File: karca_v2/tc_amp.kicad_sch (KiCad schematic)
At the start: 12 parts, among them U20 AD8495

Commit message: updated
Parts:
- removed C28: 0.82u, Capacitor_SMD:C_1206_3216Metric, symbol Device:C
- removed L6: 4.7m, symbol Device:L
- added C9: 0.075u, Capacitor_SMD:C_1206_3216Metric, symbol Device:C
- added Ce1: 0.15u, Capacitor_SMD:C_1206_3216Metric, symbol Device:C
- added D25: D_Schottky, Diode_SMD:D_SMA, symbol Device:D_Schottky
- added D58, D62: TVS0701, symbol Device:D_TVS
- added R61: 1k, symbol Device:R_US
- added U43: TLV9304xD, Package_SO:SO-14_3.9x8.65mm_P1.27mm, symbol Amplifier_Operational:TLV9304xD
- R57: value 90 -> 1k
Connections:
- net +5V: now also D25.1 (K)
- net GND: now also C9.2, D58.1 (A1), D62.1 (A1)
- net IN_1: now also D58.2 (A2)
- net IN_2: now also D62.2 (A2)
- net V_OUT: now also Ce1.1, D25.2 (A), U43.6 (-), U43.7
- net at R57.2: now also Ce1.2, R61.1
- new net: C9.1, R61.2, U43.5 (+)
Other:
- note added: "fc = 1.5kHz"
- note removed: "Inductor has 20 ohms of resistance"
- note removed: "fc = 2.5kHz"

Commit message: Version alpha
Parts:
- removed D25: D_Schottky, Diode_SMD:D_SMA, symbol Device:D_Schottky
- removed D58, D62: TVS0701, symbol Device:D_TVS
- added R116: 1k, Resistor_SMD:R_1206_3216Metric, symbol Device:R_US
- added U25: ~, Package_SON:VSON-8-1EP_3x3mm_P0.65mm_EP1.65x2.4mm_ThermalVias, symbol karca_lib:TVS0701-7V
- added U39: ~, Package_TO_SOT_SMD:SOT-23-5, symbol karca_lib:TLVH431
- C26, C29: footprint Capacitor_SMD:C_1210_3225Metric -> Capacitor_SMD:C_1206_3216Metric
- R57: renamed from R56; footprint (none) -> Resistor_SMD:R_1206_3216Metric
- R58: renamed from R57; footprint (none) -> Resistor_SMD:R_1206_3216Metric
- R59: renamed from R61; footprint (none) -> Resistor_SMD:R_1206_3216Metric
- R60: renamed from R58; footprint (none) -> Resistor_SMD:R_1206_3216Metric
- R61: renamed from R59; footprint (none) -> Resistor_SMD:R_1206_3216Metric
- renumbered C9 to C28, U43 to U13, U20 to U24
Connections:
- net +5V: now also R116.2
- net GND: now also U25.5 (GND), U25.6 (GND), U39.5 (A); no longer U24.2 (REF)
- net IN_1: now also U25.1 (IN)
- net IN_2: now also U25.2 (IN)
- new net: R116.1, U24.2 (REF), U39.3 (C), U39.4 (REF)
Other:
- note removed: "Vref set to 0V since only +ve temperatures will be measured"
- moved on the sheet: C25, C26, C27, C28, C29, C30, Ce1, R57, R58, R59, R60, R61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

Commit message: discrete traces
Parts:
- renumbered C25 to C40, C26 to C41, C27 to C42, C28 to C43, C29 to C44, C30 to C45, R116 to R62, U24 to U30, U25 to U31, U39 to U37

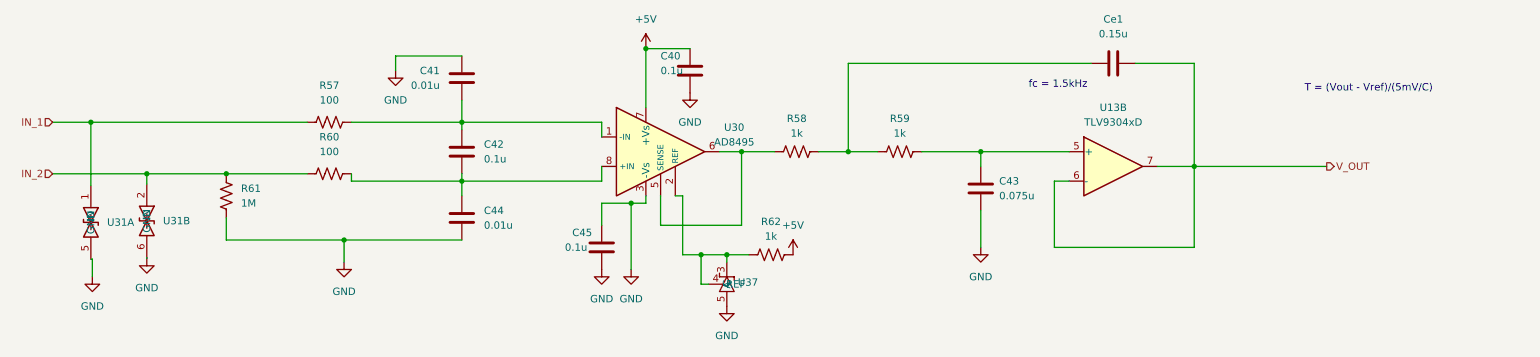
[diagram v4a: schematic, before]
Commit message: fixed TVS Diodes
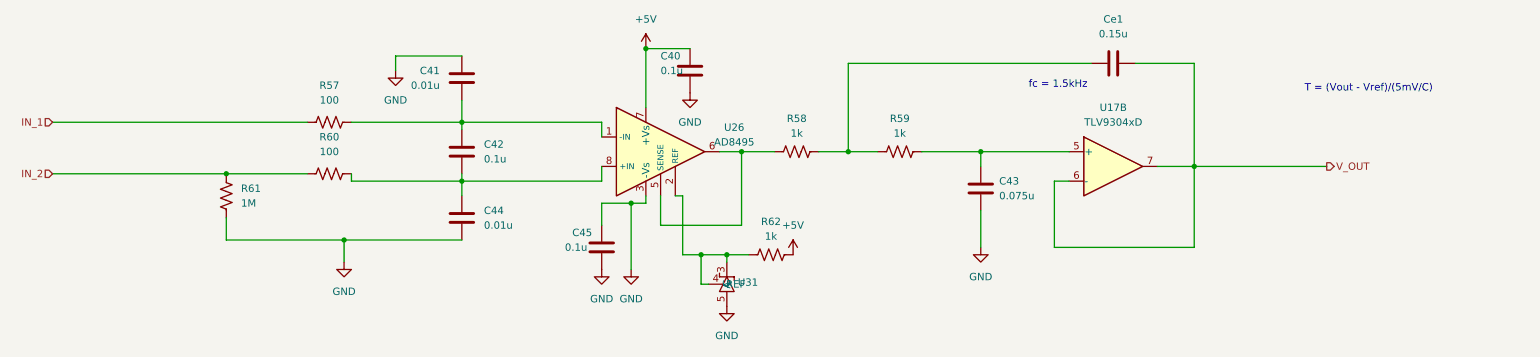
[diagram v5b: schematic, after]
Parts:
- removed U31: ~, Package_SON:VSON-8-1EP_3x3mm_P0.65mm_EP1.65x2.4mm_ThermalVias, symbol karca_lib:TVS0701-7V
- renumbered U13 to U17, U30 to U26, U37 to U31

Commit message: fixed violations
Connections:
- net in+: now reaches C42.1, C44.2, R60.2, U26.8 (+IN)
- net in-: now reaches C41.1, C42.2, R57.2, U26.1 (-IN)
- net vref: now reaches R62.1, U26.2 (REF), U31.3 (C), U31.4 (REF)
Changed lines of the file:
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@@
+    (effects (font (size 1.27 1.27)) (justify left bottom))
+  )
+  (label "vref" (at 140.97 62.23 0) (fields_autoplaced)
+    (effects (font (size 1.27 1.27)) (justify left bottom))
+  )
+  (label "in-" (at 125.095 49.53 0) (fields_autoplaced)
+    (effects (font (size 1.27 1.27)) (justify left bottom))
+  )
+  (label "in+" (at 123.825 59.69 0) (fields_autoplaced)
     (effects (font (size 1.27 1.27)) (justify left bottom))
   )

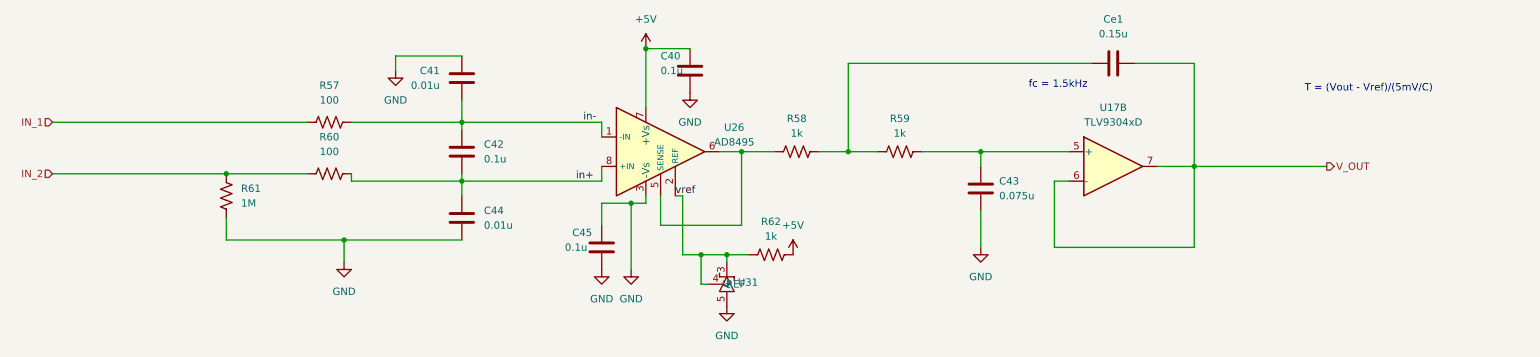
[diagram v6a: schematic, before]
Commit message: Fixed ground capacitors
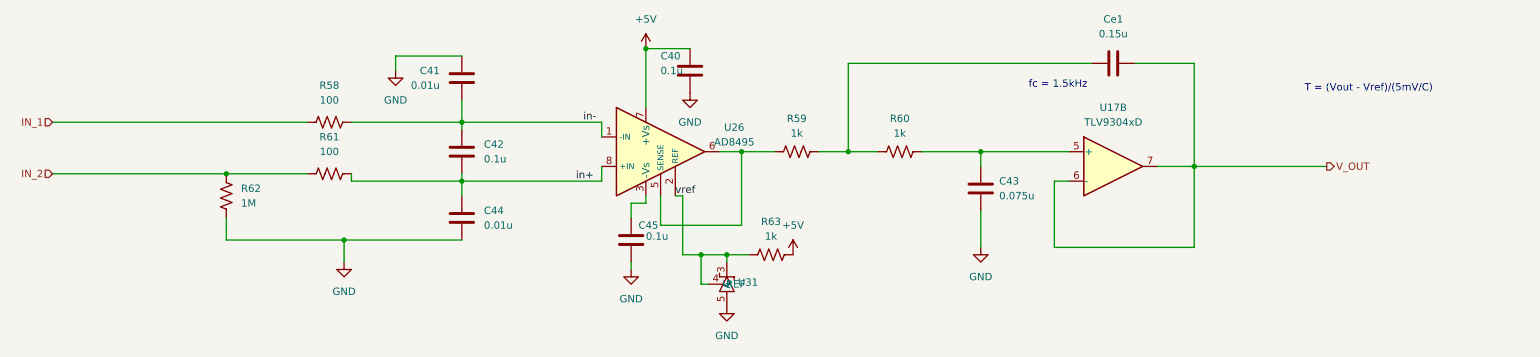
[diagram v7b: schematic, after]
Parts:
- renumbered R57 to R58, R58 to R59, R59 to R60, R60 to R61, R61 to R62, R62 to R63
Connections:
- net GND: no longer C45.2, U26.3 (-Vs)
- new net: C45.2, U26.3 (-Vs)

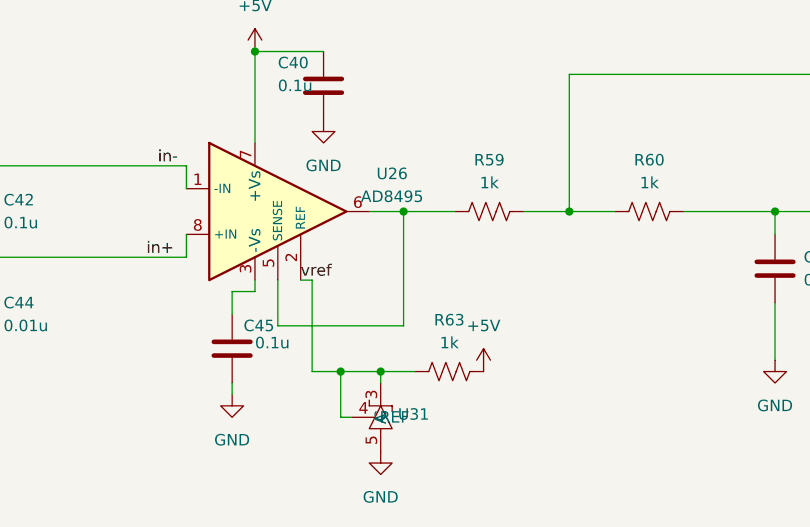
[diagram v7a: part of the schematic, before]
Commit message: Passed all DRC, Added safety jumper to isolate regulators from rest of the board
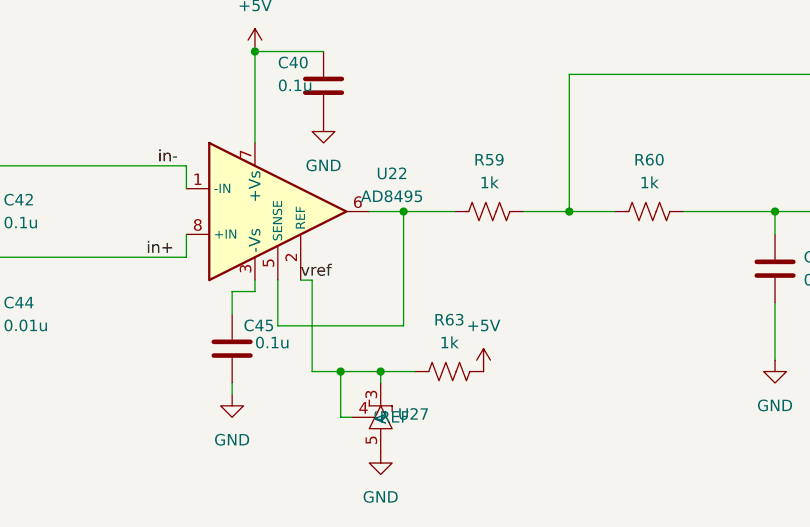
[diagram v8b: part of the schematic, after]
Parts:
- renumbered U26 to U22, U31 to U27
